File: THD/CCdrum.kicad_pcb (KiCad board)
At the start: 2 copper layers, 106 x 54.5 mm, 39 parts, among them J1 Barrel_Jack, J4 IN, J5 OUT, Q1 BC557, SW1 SW_Push, SW2 SW_Push, U1 MSP430G2533, U2 LM1117IMP-3.3, U3 6N139

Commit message: changed buffer
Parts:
- removed Q1: BC557, Package_TO_SOT_THT:TO-92_HandSolder
- removed R6: 47k, Resistor_THT:R_Axial_DIN0207_L6.3mm_D2.5mm_P7.62mm_Horizontal
- added U4: 74HC14, Package_DIP:DIP-14_W7.62mm, F.Cu at (138.2, 123.9)
- J4: value IN -> MIDI_in
- J5: value OUT -> MIDI_out
- moved R2 17.1 mm to (114.1, 117.2)
- moved R8 15.3 mm to (119.0, 123.9), turned to 270 degrees
- moved U3 3.80 mm to (115.2, 123.9)
- moved R9 3.17 mm to (103.8, 131.6)
- moved R3 2.54 mm to (100.0, 131.6)
- moved D1 1.85 mm to (96.7, 127.8)
- moved J5 1.23 mm to (125.4, 113.0)
- moved J4 1.20 mm to (102.8, 113.2)
- moved R11 1.17 mm to (93.3, 123.9)
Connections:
- RV1 pad : GND -> (no net)
- RV2 pad : GND -> (no net)
- RV3 pad : GND -> (no net)
- RV4 pad : GND -> (no net)
- RV5 pad : GND -> (no net)
- RV6 pad : GND -> (no net)
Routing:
- net TXD: track 82.2 -> 58.8 mm
- net +3V3: track 206.3 -> 219.7 mm
- net Net-(R8-Pad2): track 12.1 -> 3.94 mm
- net Net-(J5-Pad4): track 14.6 -> 6.84 mm
- net Net-(U4-Pad6): track 0.00 -> 7.62 mm
- net Net-(J4-Pad4): track 12.8 -> 6.18 mm
- net Net-(D1-Pad1): track 25.2 -> 19.2 mm
- net PUSH_L2: track 84.6 -> 90.2 mm, vias 2 -> 3
- net RXD: track 51.8 -> 47.2 mm, vias 2 -> 1
- net Net-(D1-Pad2): track 19.9 -> 24.1 mm, vias 0 -> 1
- net Net-(J5-Pad5): track 17.1 -> 13.6 mm
- net PUSH_L1: track 71.1 -> 73.3 mm
- net LED_P5: track 8.20 -> 6.96 mm
- net Net-(D6-Pad2): track 28.0 -> 29.1 mm

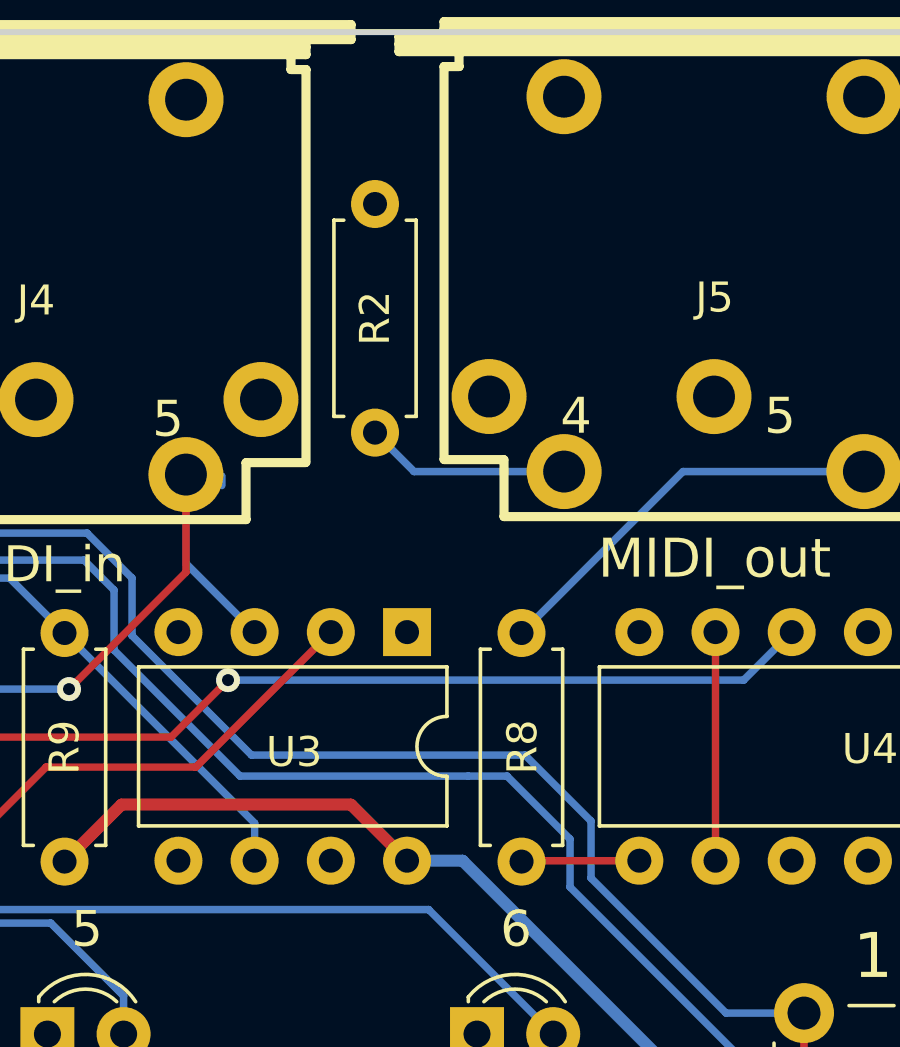
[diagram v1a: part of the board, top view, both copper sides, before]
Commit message: Changed the MIDI out pullup resistor
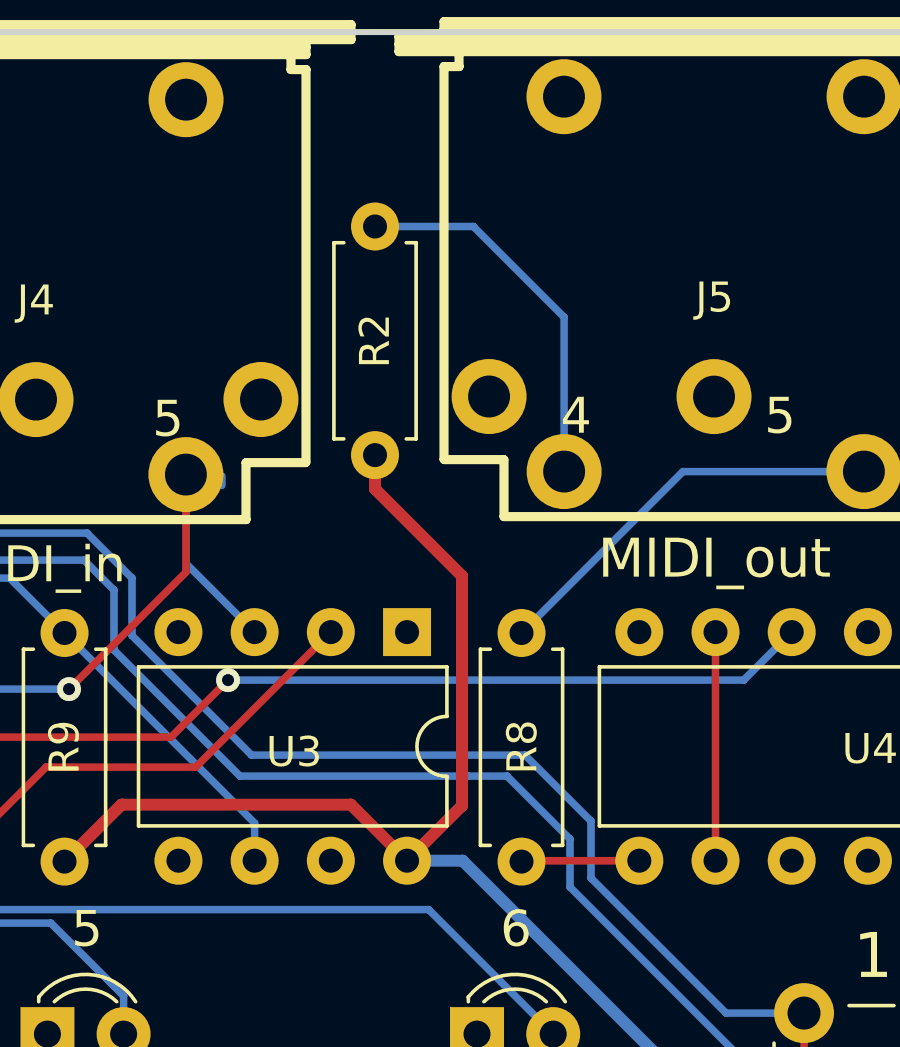
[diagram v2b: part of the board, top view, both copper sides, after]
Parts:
- moved R2 0.75 mm to (114.1, 118.0)
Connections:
- R2 pad 1: Net-(J5-Pad4) -> +3V3
- R2 pad 2: GND -> Net-(J5-Pad4)
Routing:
- net +3V3: track 219.7 -> 235.2 mm
- net Net-(J5-Pad4): track 6.84 -> 12.7 mm
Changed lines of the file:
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@@
     (thickness 1.6)
     (drawings 63)
-    (tracks 267)
+    (tracks 272)
     (zones 0)
     (modules 38)
@@
   )
   (module Resistor_THT:R_Axial_DIN0207_L6.3mm_D2.5mm_P7.62mm_Horizontal (layer F.Cu)
-    (at 114.1 117.25 90)
+    (at 114.1 118 90)
     (descr "Resistor, Axial_DIN0207 series, Axial, Horizontal, pin pitch=7.62mm, 0.25W = 1/4W, length*diameter=6.3*2.5mm^2, http://cdn-reichelt.de/documents/datenblatt/B400/1_4W%23YAG.pdf")
     (tags "Resistor Axial_DIN0207 series Axial Horizontal pin pitch 7.62mm 0.25W = 1/4W length 6.3mm diameter 2.5mm")
@@
     (fp_line (start 0.66 -1.25) (end 0.66 1.25) (layer F.Fab) (width 0.1))
     (pad 2 thru_hole oval (at 7.62 0 90) (size 1.6 1.6) (drill 0.8) (layers *.Cu *.Mask)
-      (net 1 GND))
+      (net 28 "Net-(J5-Pad4)"))
     (pad 1 thru_hole circle (at 0 0 90) (size 1.6 1.6) (drill 0.8) (layers *.Cu *.Mask)
-      (net 28 "Net-(J5-Pad4)"))
+      (net 5 +3V3))
     (model ${KISYS3DMOD}/Resistor_THT.3dshapes/R_Axial_DIN0207_L6.3mm_D2.5mm_P7.62mm_Horizontal.wrl
       (at (xyz 0 0 0))
@@
   (segment (start 113.297332 129.65) (end 115.167332 131.52) (width 0.4) (layer F.Cu) (net 5))
   (segment (start 105.650999 129.65) (end 113.297332 129.65) (width 0.4) (layer F.Cu) (net 5))
+  (segment (start 114.1 119.13137) (end 117 122.03137) (width 0.4) (layer F.Cu) (net 5))
+  (segment (start 114.1 118) (end 114.1 119.13137) (width 0.4) (layer F.Cu) (net 5))
+  (segment (start 117 129.687332) (end 115.167332 131.52) (width 0.4) (layer F.Cu) (net 5))
+  (segment (start 117 122.03137) (end 117 129.687332) (width 0.4) (layer F.Cu) (net 5))
   (segment (start 127.99 123.9) (end 126.39 125.5) (width 0.25) (layer B.Cu) (net 6))
   (segment (start 126.39 125.5) (end 109.2 125.5) (width 0.25) (layer B.Cu) (net 6))
@@
   (segment (start 130.6 144.5) (end 130.6 138.6) (width 0.25) (layer F.Cu) (net 26))
   (segment (start 128.4 146.7) (end 130.6 144.5) (width 0.25) (layer F.Cu) (net 26))
-  (segment (start 115.3991 118.5491) (end 114.1 117.25) (width 0.25) (layer B.Cu) (net 28))
-  (segment (start 120.40382 118.5491) (end 115.3991 118.5491) (width 0.25) (layer B.Cu) (net 28))
+  (segment (start 117.38 110.38) (end 114.1 110.38) (width 0.25) (layer B.Cu) (net 28))
+  (segment (start 120.40382 118.5491) (end 120.40382 113.40382) (width 0.25) (layer B.Cu) (net 28))
+  (segment (start 120.40382 113.40382) (end 117.38 110.38) (width 0.25) (layer B.Cu) (net 28))
   (segment (start 99.984666 120.829946) (end 99.984666 123.93) (width 0.25) (layer F.Cu) (net 33))
   (segment (start 97.80382 118.6491) (end 99.984666 120.829946) (width 0.25) (layer F.Cu) (net 33))

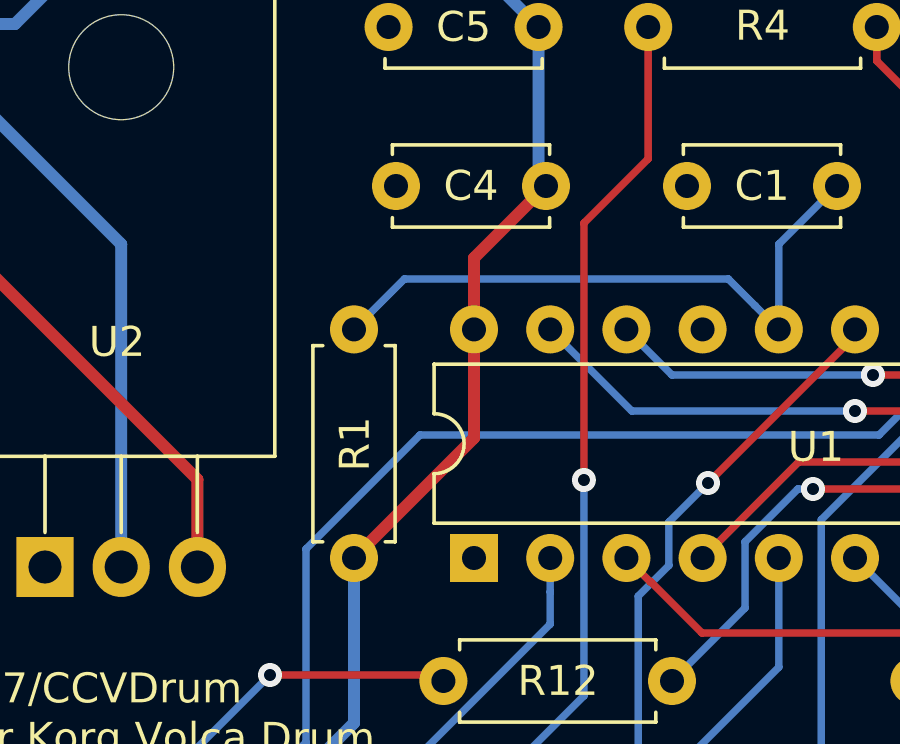
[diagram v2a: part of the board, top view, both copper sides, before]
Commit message: Fixed the mcu supply
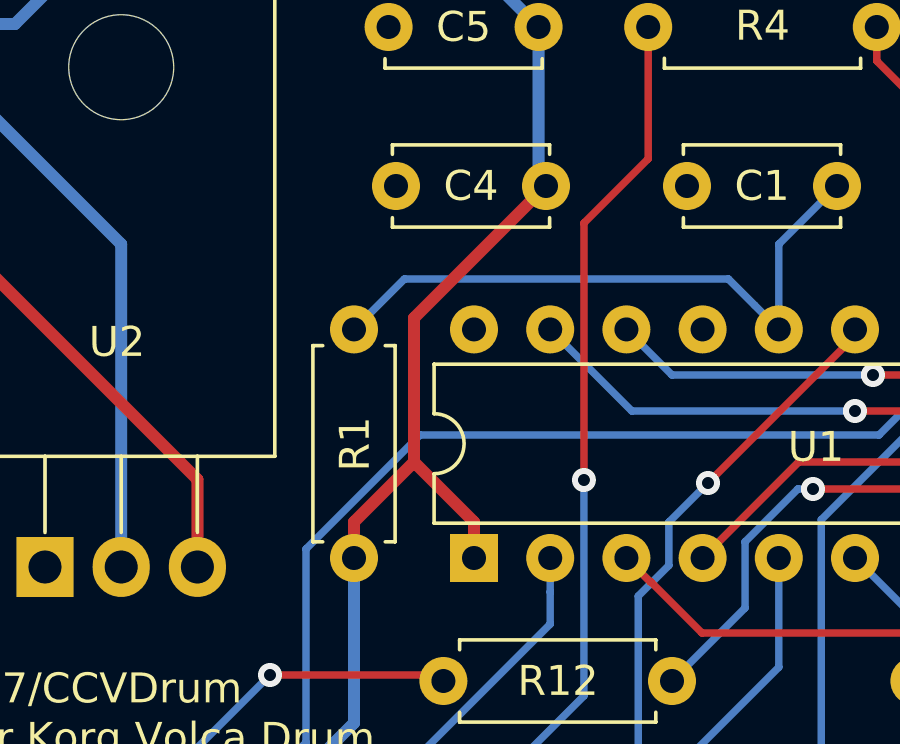
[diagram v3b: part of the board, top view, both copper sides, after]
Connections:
- U1 pad 1: GND -> +3V3
- U1 pad 20: +3V3 -> GND
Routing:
- net +3V3: track 235.2 -> 239.2 mm
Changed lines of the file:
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@@
     (thickness 1.6)
     (drawings 63)
-    (tracks 272)
+    (tracks 274)
     (zones 0)
     (modules 38)
@@
     (fp_arc (start 3.81 -1.33) (end 2.81 -1.33) (angle -180) (layer F.SilkS) (width 0.12))
     (pad 20 thru_hole oval (at 7.62 0 90) (size 1.6 1.6) (drill 0.8) (layers *.Cu *.Mask)
-      (net 5 +3V3))
+      (net 1 GND))
     (pad 10 thru_hole oval (at 0 22.86 90) (size 1.6 1.6) (drill 0.8) (layers *.Cu *.Mask)
       (net 21 LED_P4))
@@
       (net 22 LED_P3))
     (pad 1 thru_hole rect (at 0 0 90) (size 1.6 1.6) (drill 0.8) (layers *.Cu *.Mask)
-      (net 1 GND))
+      (net 5 +3V3))
     (model ${KISYS3DMOD}/Package_DIP.3dshapes/DIP-20_W7.62mm.wrl
       (at (xyz 0 0 0))
@@
   (segment (start 54.84 125.5) (end 54.84 114.74) (width 0.4) (layer B.Cu) (net 5))
   (segment (start 68.753333 112.553333) (end 69 112.8) (width 0.4) (layer F.Cu) (net 5))
-  (segment (start 66.6 115.2) (end 66.6 117.58) (width 0.4) (layer F.Cu) (net 5))
-  (segment (start 69 112.8) (end 66.6 115.2) (width 0.4) (layer F.Cu) (net 5))
-  (segment (start 66.6 121.2) (end 62.6 125.2) (width 0.4) (layer F.Cu) (net 5))
-  (segment (start 66.6 117.58) (end 66.6 121.2) (width 0.4) (layer F.Cu) (net 5))
   (segment (start 62.6 125.2) (end 62.6 130.7) (width 0.4) (layer B.Cu) (net 5))
   (segment (start 49.7 143.6) (end 49.7 145.4) (width 0.4) (layer B.Cu) (net 5))
@@
   (segment (start 117 129.687332) (end 115.167332 131.52) (width 0.4) (layer F.Cu) (net 5))
   (segment (start 117 122.03137) (end 117 129.687332) (width 0.4) (layer F.Cu) (net 5))
+  (segment (start 66.6 124) (end 64.6 122) (width 0.4) (layer F.Cu) (net 5))
+  (segment (start 66.6 125.2) (end 66.6 124) (width 0.4) (layer F.Cu) (net 5))
+  (segment (start 64.6 117.2) (end 69 112.8) (width 0.4) (layer F.Cu) (net 5))
+  (segment (start 64.6 122) (end 64.6 117.2) (width 0.4) (layer F.Cu) (net 5))
+  (segment (start 62.6 124) (end 64.6 122) (width 0.4) (layer F.Cu) (net 5))
+  (segment (start 62.6 125.2) (end 62.6 124) (width 0.4) (layer F.Cu) (net 5))
   (segment (start 127.99 123.9) (end 126.39 125.5) (width 0.25) (layer B.Cu) (net 6))
   (segment (start 126.39 125.5) (end 109.2 125.5) (width 0.25) (layer B.Cu) (net 6))
